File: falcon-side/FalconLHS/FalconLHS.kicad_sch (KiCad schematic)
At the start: 9 parts, among them U1 AL8843QSP-13

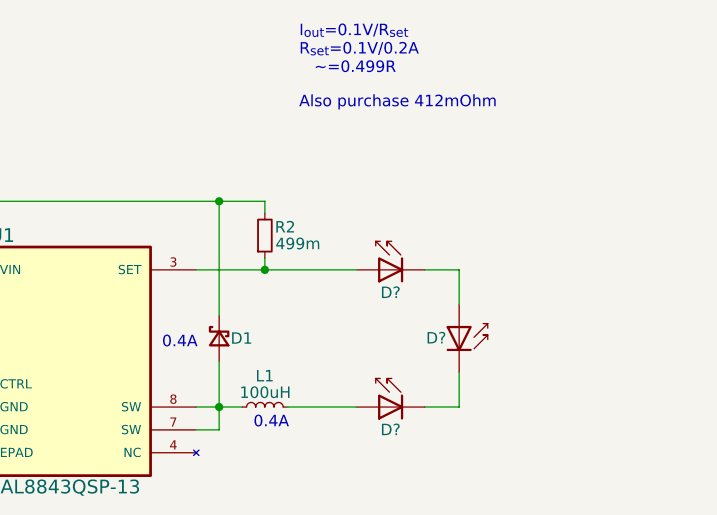
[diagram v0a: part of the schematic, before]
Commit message: PMOS diode replacement
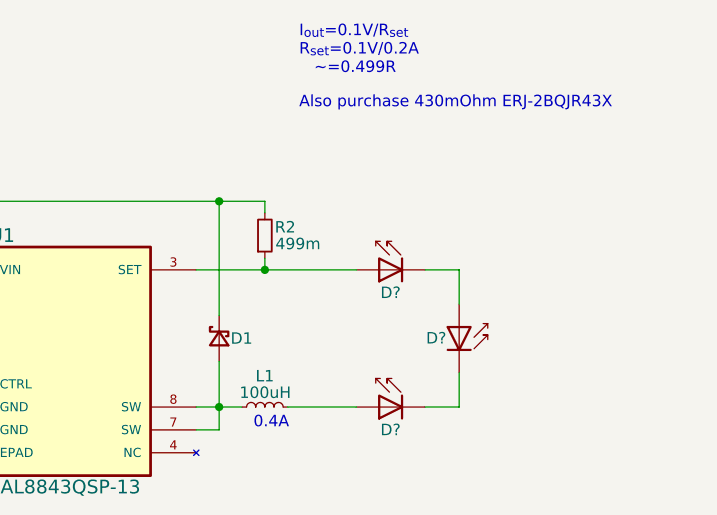
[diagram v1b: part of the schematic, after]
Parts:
- C1: footprint (none) -> Capacitor_SMD:C_1210_3225Metric; Manufacturer (none) -> TDK Corporation; Part Number (none) -> CGA6P3X7S1H106K250AB; Temp Range (none) -> -55°C +125°C; Tolerance (none) -> 10%; Voltage (none) -> 50V
- D1: value D_Schottky_Small -> 500mA; Manufacturer (none) -> Toshiba Semiconductor and Storage; Part Number (none) -> CUS551V30,H3F; Temp Range (none) -> -55°C +125°C
- L1: Manufacturer (none) -> Taiyo Yuden; Part Number (none) -> NR6028T101M; Temp Range (none) -> -25°C +120°C; Tolerance (none) -> 20%
- R1: footprint (none) -> Resistor_SMD:R_0402_1005Metric; Manufacturer (none) -> Stackpole Electronics Inc; Part Number (none) -> RMCF0402FT1M00; Temp Range (none) -> -55°C +155°C; Tolerance (none) -> 1%
- R2: footprint (none) -> Resistor_SMD:R_0402_1005Metric; Manufacturer (none) -> YAGEO; Part Number (none) -> RL0402FR-070R499L; Power (none) -> 0.063W; Temp Range (none) -> -55°C +155°C; Tolerance (none) -> 1%
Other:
- note added: "Also purchase 430mOhm ERJ-2BQJR43X"
- note removed: "Also purchase 412mOhm"
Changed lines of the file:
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@@
     (stroke (width 0) (type default) (color 0 0 0 0))
   )
-  (text "Also purchase 412mOhm" (at 116.84 46.99 0)
+  (text "Also purchase 430mOhm ERJ-2BQJR43X" (at 116.84 46.99 0)
     (effects (font (size 1.27 1.27)) (justify left bottom))
   )
@@
   )
   (text "0.4A" (at 111.76 82.55 0)
-    (effects (font (size 1.27 1.27)) (justify left bottom))
-  )
-  (text "0.4A" (at 101.6 73.66 0)
     (effects (font (size 1.27 1.27)) (justify left bottom))
   )
@@
       (effects (font (size 1.27 1.27)) (justify right))
     )
-    (property "Footprint" "" (id 2) (at 76.2 68.58 0)
-      (effects (font (size 1.27 1.27)) hide)
-    )
-    (property "Datasheet" "~" (id 3) (at 76.2 68.58 0)
+    (property "Footprint" "Capacitor_SMD:C_1210_3225Metric" (id 2) (at 76.2 68.58 0)
+      (effects (font (size 1.27 1.27)) hide)
+    )
+    (property "Datasheet" "https://product.tdk.com/system/files/dam/doc/product/capacitor/ceramic/mlcc/catalog/mlcc_automotive_general_en.pdf" (id 3) (at 76.2 68.58 0)
+      (effects (font (size 1.27 1.27)) hide)
+    )
+    (property "Description" "CAP CER 10UF 50V X7S 1210" (id 4) (at 76.2 68.58 0)
+      (effects (font (size 1.27 1.27)) hide)
+    )
+    (property "Manufacturer" "TDK Corporation" (id 5) (at 76.2 68.58 0)
+      (effects (font (size 1.27 1.27)) hide)
+    )
+    (property "Part Number" "CGA6P3X7S1H106K250AB " (id 6) (at 76.2 68.58 0)
+      (effects (font (size 1.27 1.27)) hide)
+    )
+    (property "Temp Range" "-55°C +125°C" (id 7) (at 76.2 68.58 0)
+      (effects (font (size 1.27 1.27)) hide)
+    )
+    (property "Tolerance" "10%" (id 8) (at 76.2 68.58 0)
+      (effects (font (size 1.27 1.27)) hide)
+    )
+    (property "Voltage" "50V" (id 9) (at 76.2 68.58 0)
       (effects (font (size 1.27 1.27)) hide)
     )
@@
       (effects (font (size 1.27 1.27)) hide)
     )
-    (property "Datasheet" "~" (id 3) (at 113.03 80.01 0)
+    (property "Datasheet" "https://ds.yuden.co.jp/TYCOMPAS/ut/detail?pn=LSXBD6060WHL101M&u=M" (id 3) (at 113.03 80.01 0)
+      (effects (font (size 1.27 1.27)) hide)
+    )
+    (property "Description" "FIXED IND 100UH 660MA 780MOHM SM" (id 4) (at 113.03 80.01 0)
+      (effects (font (size 1.27 1.27)) hide)
+    )
+    (property "Manufacturer" "Taiyo Yuden" (id 5) (at 113.03 80.01 0)
+      (effects (font (size 1.27 1.27)) hide)
+    )
+    (property "Part Number" "NR6028T101M" (id 6) (at 113.03 80.01 0)
+      (effects (font (size 1.27 1.27)) hide)
+    )
+    (property "Temp Range" "-25°C +120°C" (id 7) (at 113.03 80.01 0)
+      (effects (font (size 1.27 1.27)) hide)
+    )
+    (property "Tolerance" "20%" (id 8) (at 113.03 80.01 0)
       (effects (font (size 1.27 1.27)) hide)
     )
@@
       (effects (font (size 1.27 1.27)) (justify right))
     )
-    (property "Value" "D_Schottky_Small" (id 1) (at 105.41 72.136 0)
+    (property "Value" "500mA" (id 1) (at 105.41 72.136 0)
       (effects (font (size 1.27 1.27)) hide)
     )
@@
       (effects (font (size 1.27 1.27)) hide)
     )
-    (property "Datasheet" "~" (id 3) (at 107.95 72.39 90)
+    (property "Datasheet" "https://toshiba.semicon-storage.com/info/docget.jsp?did=10394&prodName=CUS551V30" (id 3) (at 107.95 72.39 90)
+      (effects (font (size 1.27 1.27)) hide)
+    )
+    (property "Description" "DIODE SCHOTTKY 30V 500MA USC" (id 4) (at 107.95 72.39 0)
+      (effects (font (size 1.27 1.27)) hide)
+    )
+    (property "Manufacturer" "Toshiba Semiconductor and Storage" (id 5) (at 107.95 72.39 0)
+      (effects (font (size 1.27 1.27)) hide)
+    )
+    (property "Part Number" "CUS551V30,H3F" (id 6) (at 107.95 72.39 0)
+      (effects (font (size 1.27 1.27)) hide)
+    )
+    (property "Temp Range" "-55°C +125°C" (id 7) (at 107.95 72.39 0)
       (effects (font (size 1.27 1.27)) hide)
     )
@@
       (effects (font (size 1.27 1.27)) (justify right))
     )
-    (property "Footprint" "" (id 2) (at 73.66 81.28 0)
-      (effects (font (size 1.27 1.27)) hide)
-    )
-    (property "Datasheet" "~" (id 3) (at 73.66 81.28 0)
+    (property "Footprint" "Resistor_SMD:R_0402_1005Metric" (id 2) (at 73.66 81.28 0)
+      (effects (font (size 1.27 1.27)) hide)
+    )
+    (property "Datasheet" "https://www.seielect.com/catalog/sei-rmcf_rmcp.pdf" (id 3) (at 73.66 81.28 0)
+      (effects (font (size 1.27 1.27)) hide)
+    )
+    (property "Description" "RES 1M OHM 1% 1/16W 0402" (id 4) (at 73.66 81.28 0)
+      (effects (font (size 1.27 1.27)) hide)
+    )
+    (property "Manufacturer" "Stackpole Electronics Inc" (id 5) (at 73.66 81.28 0)
+      (effects (font (size 1.27 1.27)) hide)
+    )
+    (property "Part Number" "RMCF0402FT1M00" (id 6) (at 73.66 81.28 0)
+      (effects (font (size 1.27 1.27)) hide)
+    )
+    (property "Temp Range" "-55°C +155°C" (id 7) (at 73.66 81.28 0)
+      (effects (font (size 1.27 1.27)) hide)
+    )
+    (property "Tolerance" "1%" (id 8) (at 73.66 81.28 0)
       (effects (font (size 1.27 1.27)) hide)
     )
@@
       (effects (font (size 1.27 1.27)) (justify left))
     )
-    (property "Footprint" "" (id 2) (at 113.03 60.96 0)
-      (effects (font (size 1.27 1.27)) hide)
-    )
-    (property "Datasheet" "~" (id 3) (at 113.03 60.96 0)
+    (property "Footprint" "Resistor_SMD:R_0402_1005Metric" (id 2) (at 113.03 60.96 0)
+      (effects (font (size 1.27 1.27)) hide)
+    )
+    (property "Datasheet" "https://www.yageo.com/upload/media/product/productsearch/datasheet/rchip/PYu-RL_Group_521_RoHS_L_2.pdf" (id 3) (at 113.03 60.96 0)
+      (effects (font (size 1.27 1.27)) hide)
+    )
+    (property "Description" "RES 0.499 OHM 1% 1/16W 0402" (id 4) (at 113.03 60.96 0)
+      (effects (font (size 1.27 1.27)) hide)
+    )
+    (property "Manufacturer" "YAGEO" (id 5) (at 113.03 60.96 0)
+      (effects (font (size 1.27 1.27)) hide)
+    )
+    (property "Part Number" "RL0402FR-070R499L" (id 6) (at 113.03 60.96 0)
+      (effects (font (size 1.27 1.27)) hide)
+    )
+    (property "Temp Range" "-55°C +155°C" (id 7) (at 113.03 60.96 0)
+      (effects (font (size 1.27 1.27)) hide)
+    )
+    (property "Power" "0.063W" (id 8) (at 113.03 60.96 0)
+      (effects (font (size 1.27 1.27)) hide)
+    )
+    (property "Tolerance" "1%" (id 9) (at 113.03 60.96 0)
       (effects (font (size 1.27 1.27)) hide)
     )
@@
     )
     (path "/1c394162-6cae-4dfe-83f4-2e383531dd08"
-      (reference "C1") (unit 1) (value "10uF") (footprint "")
+      (reference "C1") (unit 1) (value "10uF") (footprint "Capacitor_SMD:C_1210_3225Metric")
     )
     (path "/65cf1682-9622-4b70-875c-1a1706f74daa"
-      (reference "D1") (unit 1) (value "D_Schottky_Small") (footprint "")
+      (reference "D1") (unit 1) (value "500mA") (footprint "")
     )
     (path "/945ecf06-a8ba-49f9-9a39-f83d76690957"
@@
     )
     (path "/8b89d4d8-0a7d-490f-bd27-343d4579d0a2"
-      (reference "R1") (unit 1) (value "1M") (footprint "")
+      (reference "R1") (unit 1) (value "1M") (footprint "Resistor_SMD:R_0402_1005Metric")
     )
     (path "/90e27ba5-9a91-4611-88ed-00da5039226c"
-      (reference "R2") (unit 1) (value "499m") (footprint "")
+      (reference "R2") (unit 1) (value "499m") (footprint "Resistor_SMD:R_0402_1005Metric")
     )
     (path "/ca62e31b-7c96-4024-a712-9fe5b0d43137"

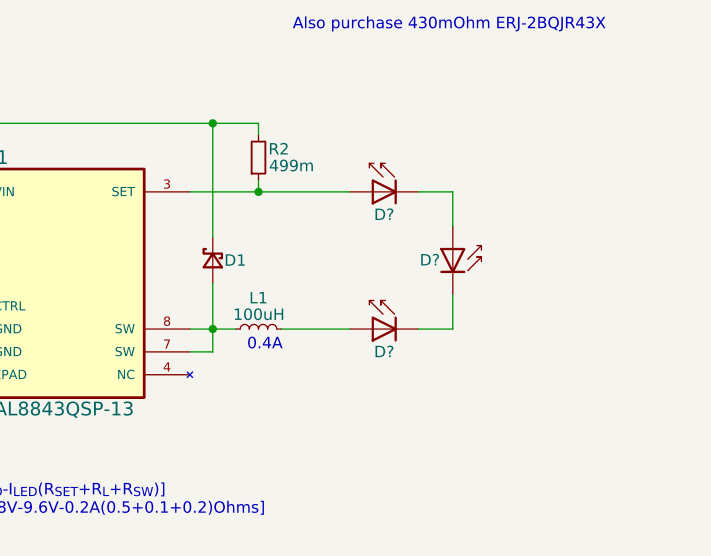
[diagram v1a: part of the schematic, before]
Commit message: Add some footprints
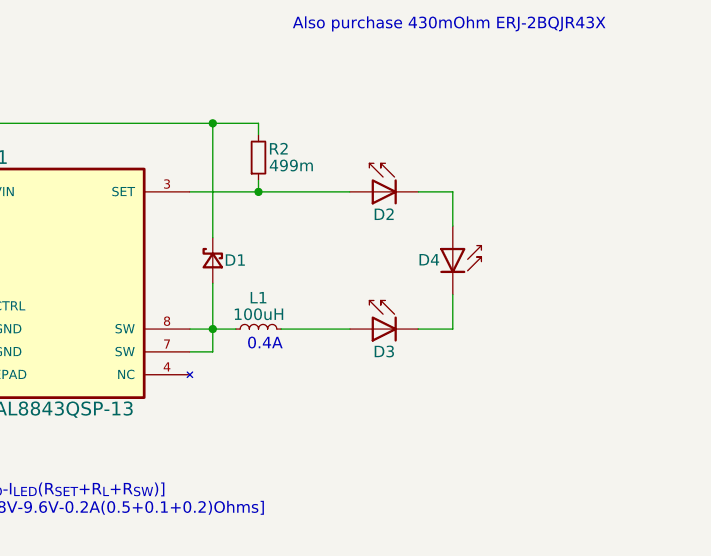
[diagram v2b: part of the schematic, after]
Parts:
- gave numbers to parts that had none: 3
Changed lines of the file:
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@@
   (symbol (lib_id "JetkovKiCADLib:XQA LED 1616 SMD") (at 125.73 64.77 0) (mirror y) (unit 1)
     (in_bom yes) (on_board yes)
-    (property "Reference" "D?" (id 0) (at 127 67.31 0))
+    (property "Reference" "D2" (id 0) (at 127 67.31 0))
     (property "Value" "XQA LED 1616 SMD" (id 1) (at 127 69.85 0)
       (effects (font (size 1.27 1.27)) hide)
@@
   (symbol (lib_id "JetkovKiCADLib:XQA LED 1616 SMD") (at 125.73 80.01 0) (mirror y) (unit 1)
     (in_bom yes) (on_board yes)
-    (property "Reference" "D?" (id 0) (at 127 82.55 0))
+    (property "Reference" "D3" (id 0) (at 127 82.55 0))
     (property "Value" "XQA LED 1616 SMD" (id 1) (at 127 85.09 0)
       (effects (font (size 1.27 1.27)) hide)
@@
   (symbol (lib_id "JetkovKiCADLib:XQA LED 1616 SMD") (at 134.62 71.12 270) (mirror x) (unit 1)
     (in_bom yes) (on_board yes)
-    (property "Reference" "D?" (id 0) (at 133.2024 72.3591 90)
+    (property "Reference" "D4" (id 0) (at 133.2024 72.3591 90)
       (effects (font (size 1.27 1.27)) (justify right))
     )
@@
     )
     (path "/945ecf06-a8ba-49f9-9a39-f83d76690957"
-      (reference "D?") (unit 1) (value "XQA LED 1616 SMD") (footprint "JetkovKiCADLib:XQ-A-LED")
+      (reference "D2") (unit 1) (value "XQA LED 1616 SMD") (footprint "JetkovKiCADLib:XQ-A-LED")
     )
     (path "/af247ce9-4d45-4565-9f3d-f7c6954a6cff"
-      (reference "D?") (unit 1) (value "XQA LED 1616 SMD") (footprint "JetkovKiCADLib:XQ-A-LED")
+      (reference "D3") (unit 1) (value "XQA LED 1616 SMD") (footprint "JetkovKiCADLib:XQ-A-LED")
     )
     (path "/d4945636-f1e7-482b-9078-24a2e696e7e3"
-      (reference "D?") (unit 1) (value "XQA LED 1616 SMD") (footprint "JetkovKiCADLib:XQ-A-LED")
+      (reference "D4") (unit 1) (value "XQA LED 1616 SMD") (footprint "JetkovKiCADLib:XQ-A-LED")
     )
     (path "/35248a03-290c-4093-81fc-ab98707d02dc"

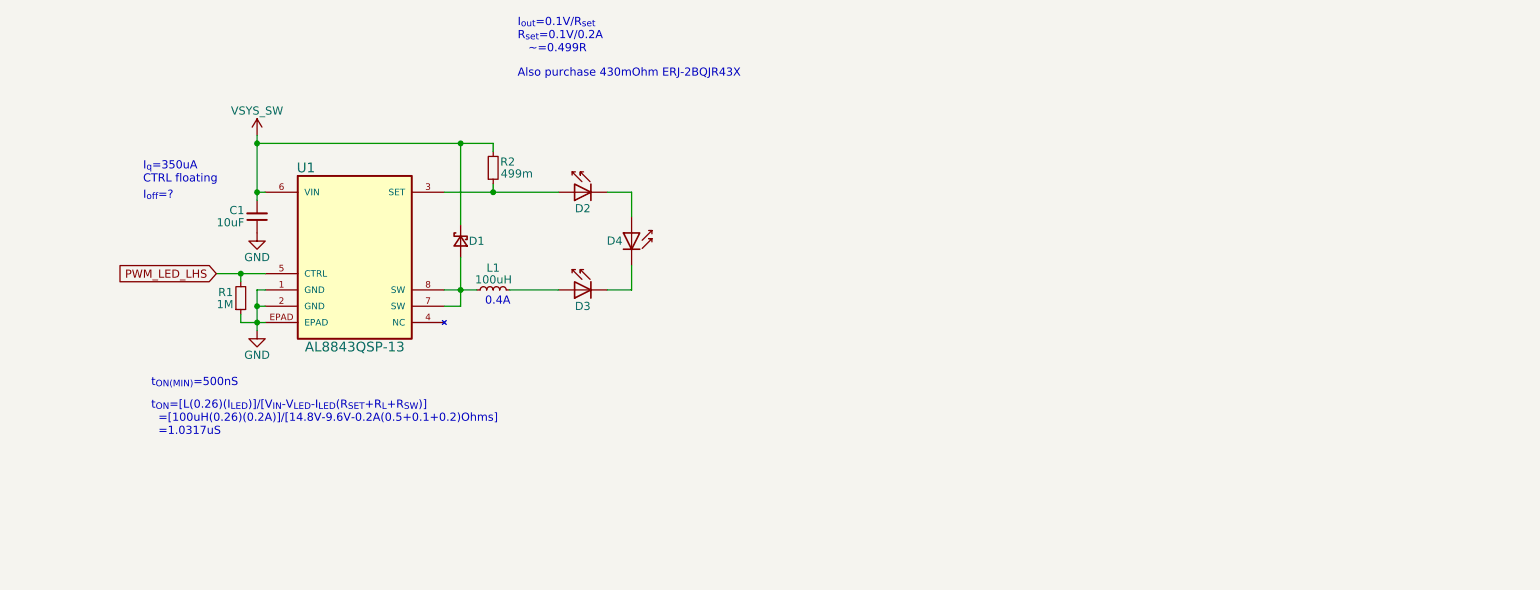
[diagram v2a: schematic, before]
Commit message: Start side board layout
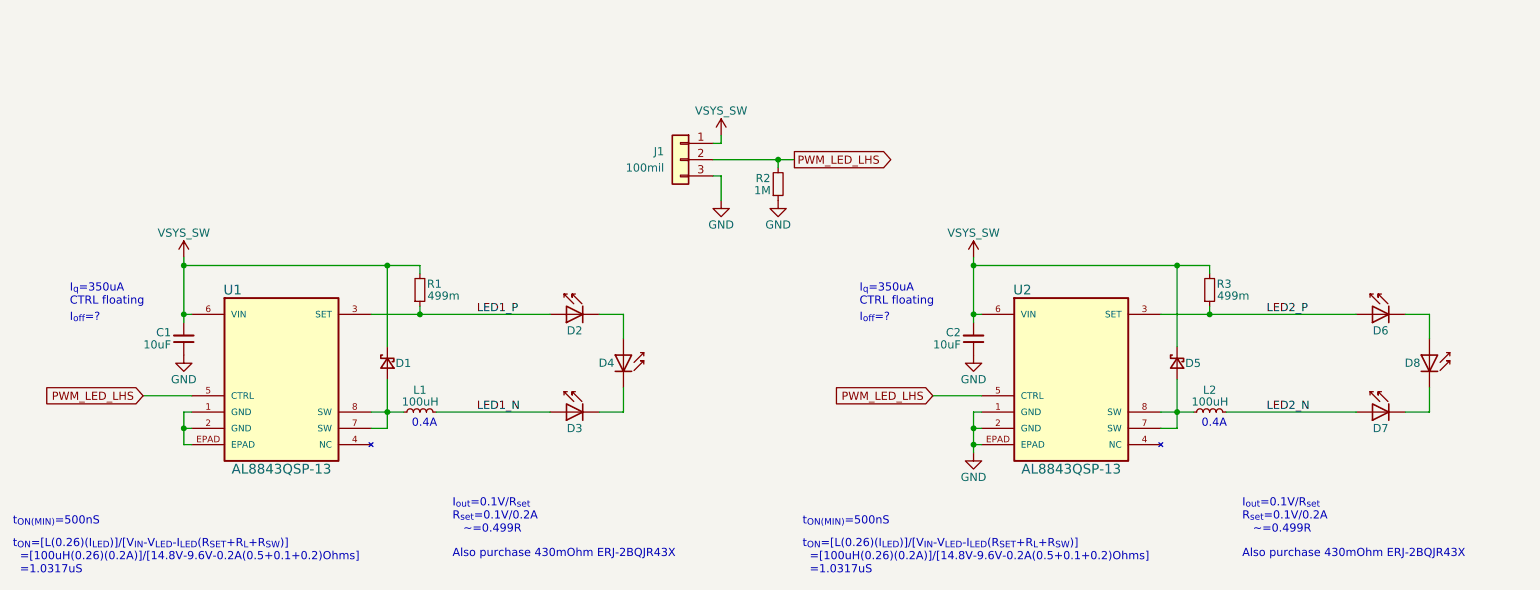
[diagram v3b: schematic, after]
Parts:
- removed R1: 1M, Resistor_SMD:R_0402_1005Metric, symbol Device:R_Small
- added C2: 10uF, Capacitor_SMD:C_1210_3225Metric, symbol Device:C_Small
- added D5: 500mA, JetkovKiCADLib:SC-76-SOD-323_USC_TSB, symbol Device:D_Schottky_Small
- added D6, D7, D8: XQA LED 1616 SMD, JetkovKiCADLib:XQ-A-LED, symbol JetkovKiCADLib:XQA LED 1616 SMD
- added J1: 100mil, Connector_PinHeader_2.54mm:PinHeader_1x03_P2.54mm_Vertical, symbol Connector_Generic:Conn_01x03
- added L2: 100uH, JetkovKiCADLib:L_Taiyo-Yuden_NR-60xx_HandSoldering, symbol Device:L_Small
- added R2: 1M, Resistor_SMD:R_0402_1005Metric, symbol Device:R_Small
- added R3: 499m, Resistor_SMD:R_0402_1005Metric, symbol Device:R_Small
- added U2: AL8843QSP-13, JetkovKiCADLib:8-SOIC_SO-8EP_DIO, symbol JetkovKiCADLib:AL8843QSP-13
- D1: footprint (none) -> JetkovKiCADLib:SC-76-SOD-323_USC_TSB
- D2, D3, D4: Part Number (none) -> XQAAPA-02-0000-000000Y01; Voltage (none) -> 3.4Vf
- L1: footprint (none) -> JetkovKiCADLib:L_Taiyo-Yuden_NR-60xx_HandSoldering
- renumbered R2 to R1
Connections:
- net GND: now also C2.1, J1.3 (Pin_3), R2.1, U2.1 (GND), U2.2 (GND), U2.EPAD; no longer U1.1 (GND), U1.2 (GND), U1.EPAD
- net PWM_LED_LHS: now also J1.2 (Pin_2), R2.2, U2.5 (CTRL)
- net VSYS_SW: now also C2.2, D5.1 (K), J1.1 (Pin_1), R3.2, U2.6 (VIN)
- net LED1_N: now reaches D3.2 (A), L1.2
- net LED1_P: now reaches D2.2 (A), R1.1, U1.3 (SET)
- new net: D7.1 (K), D8.1 (K)
- new net: U1.1 (GND), U1.2 (GND), U1.EPAD
- new net: D5.2 (A), L2.1, U2.7 (SW), U2.8 (SW)
- new net: D6.1 (K), D8.2 (A)
- new net LED2_N: D7.2 (A), L2.2
- new net LED2_P: D6.2 (A), R3.1, U2.3 (SET)
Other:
- moved on the sheet: C1, D1, D2, D3, D4, L1, R1, U1
